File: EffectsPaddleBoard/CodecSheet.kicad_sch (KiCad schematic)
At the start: 1 part, among them U3 TLV320AIC3100

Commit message: Added power to uC, but overall power not finished
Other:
- company: (none) -> Selbstständig
- title: (none) -> Effects Paddle
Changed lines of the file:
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@@
 (kicad_sch (version 20230121) (generator eeschema)
   (paper "A4")
+  (title_block
+    (title "Effects Paddle")
+    (date "2023-07-01")
+    (rev "0.1")
+    (company "Selbstständig")
+  )
   (symbol (lib_id "Audio:TLV320AIC3100") (at 158.75 99.06 0) (unit 1)
     (in_bom yes) (on_board yes) (dnp no) (fields_autoplaced)

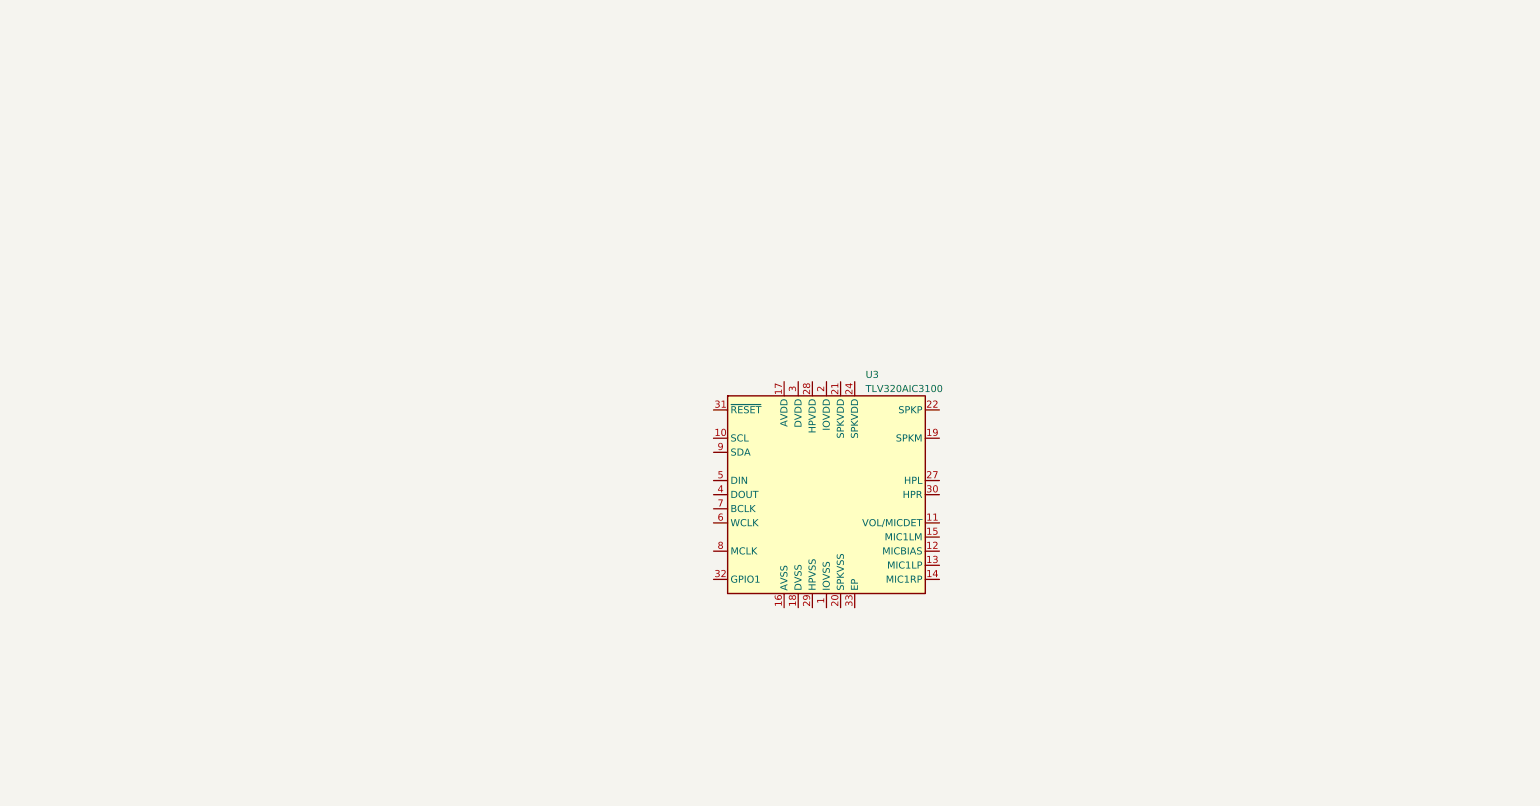
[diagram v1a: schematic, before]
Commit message: While wiring the codec, I found that I used the wrong controller and so I2S communication is unidirectional only: TODO: fix that
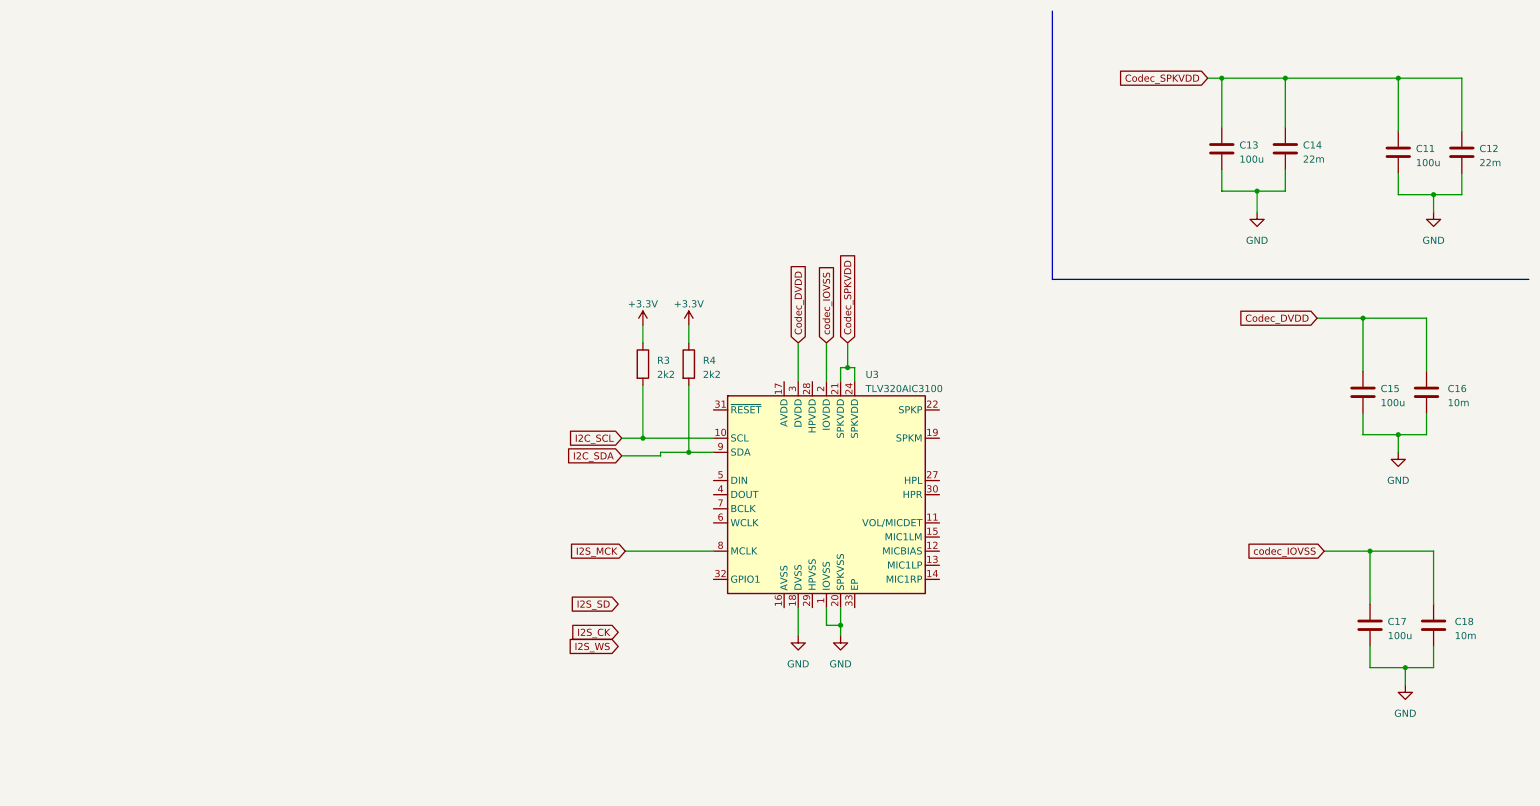
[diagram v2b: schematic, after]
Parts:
- added C11, C13, C15, C17: 100u, symbol Device:C
- added C12, C14: 22m, symbol Device:C
- added C16, C18: 10m, symbol Device:C
- added R3, R4: 2k2, symbol Device:R
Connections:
- net GND: now reaches U3.1 (IOVSS)
- net GND: now also U3.18 (DVSS), U3.20 (SPKVSS), U3.25 (SPKVSS), C11.2, C12.2, C13.2, C14.2, C15.2, C16.2, C17.2, C18.2
- net I2C_SCL: now reaches U3.10 (SCL)
- net I2C_SCL: now also R3.2
- net codec_IOVSS: now reaches U3.2 (IOVDD)
- net codec_IOVSS: now also C17.1, C18.1
- net Codec_SPKVDD: now reaches U3.21 (SPKVDD)
- net Codec_SPKVDD: now also U3.24 (SPKVDD), C11.1, C12.1, C13.1, C14.1
- net Codec_DVDD: now reaches U3.3 (DVDD)
- net Codec_DVDD: now also C15.1, C16.1
- net I2S_MCK: now reaches U3.8 (MCLK)
- net I2C_SDA: now reaches U3.9 (SDA)
- net I2C_SDA: now also R4.2
- new net +3.3V: R3.1, R4.1

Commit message: Added power supply
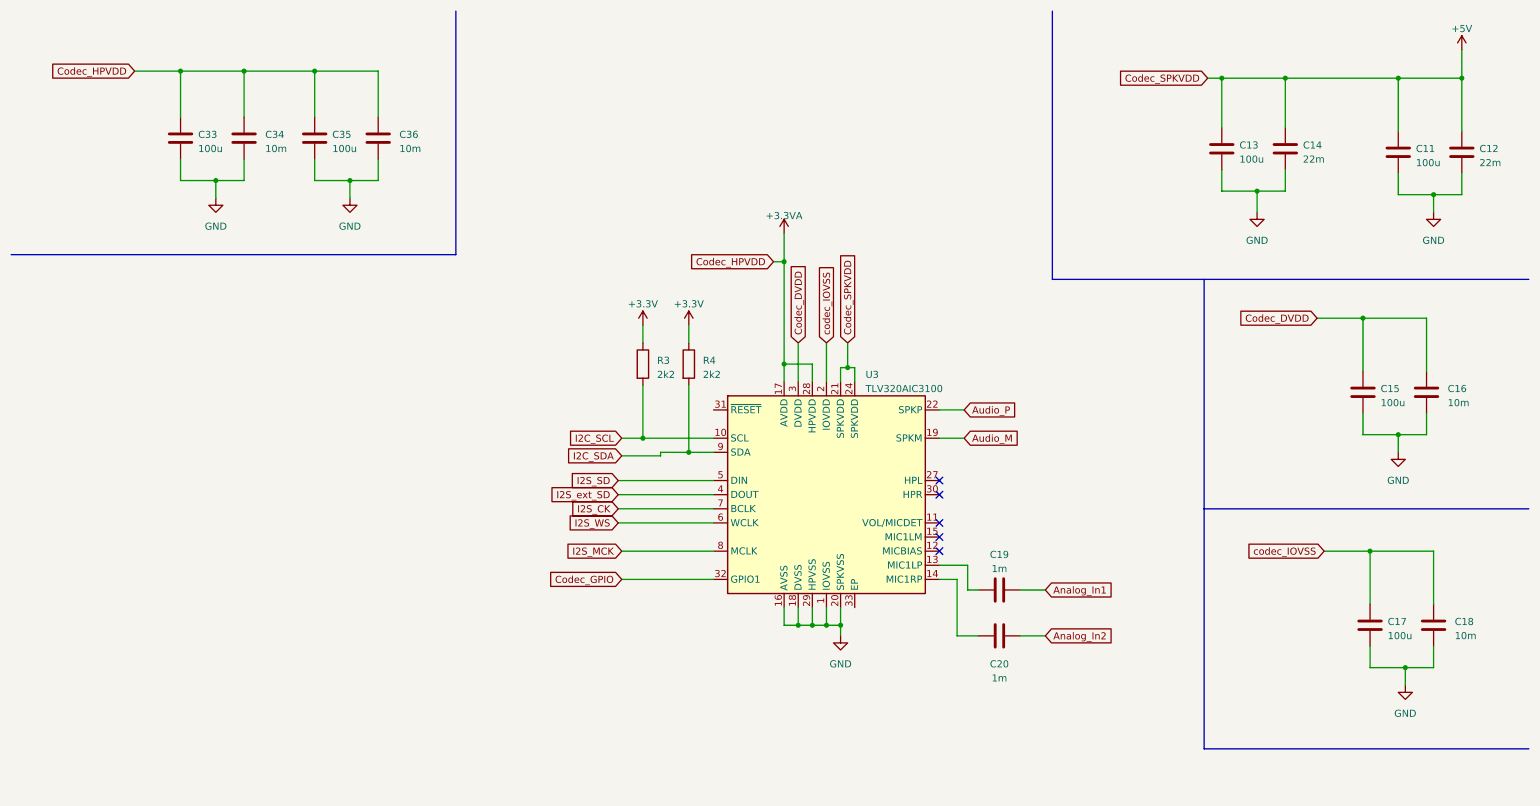
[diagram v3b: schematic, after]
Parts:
- added C19, C20: 1m, symbol Device:C
- added C33, C35: 100u, symbol Device:C
- added C34, C36: 10m, symbol Device:C
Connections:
- net GND: now also U3.16 (AVSS), U3.29 (HPVSS), C33.2, C34.2, C35.2, C36.2
- net I2S_CK: now also U3.7 (BCLK)
- net I2S_SD: now also U3.5 (DIN)
- net I2S_WS: now also U3.6 (WCLK)
- net at U3.13 (MIC1LP): now also C19.1
- net at U3.14 (MIC1RP): now also C20.1
- net +3.3VA: now reaches U3.17 (AVDD)
- net +3.3VA: now also U3.28 (HPVDD), C33.1, C34.1, C35.1, C36.1
- net Audio_M: now reaches U3.19 (SPKM), U3.23 (SPKM)
- net Audio_P: now reaches U3.22 (SPKP), U3.26 (SPKP)
- net Codec_GPIO: now reaches U3.32 (GPIO1)
- net I2S_ext_SD: now reaches U3.4 (DOUT)
- net Codec_SPKVDD renamed +5V
- new net Analog_In1: C19.2
- new net Analog_In2: C20.2
- no-connect marks 0 -> 5

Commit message: Finished schematic
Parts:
- added R16, R17, R18, R19, R20: 10k, symbol Device:R
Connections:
- net codec_IOVSS is gone; now on net +3.3V: C17.1, C18.1, U3.2 (IOVDD)
- net GND: now also R16.2, R17.2, R18.2, R19.2, R20.2
- net at U3.11 (VOL/MICDET): now also R18.1
- net at U3.12 (MICBIAS): now also R16.1
- net at U3.15 (MIC1LM): now also R17.1
- net at U3.27 (HPL): now also R20.1
- net at U3.30 (HPR): now also R19.1
- net Codec_DVDD renamed +1V8
- no-connect marks 5 -> 0
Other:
- moved on the sheet: C19, C20, R3, R4, U3

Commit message: Began with pcb layout
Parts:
- C11: footprint (none) -> Capacitor_SMD:C_0402_1005Metric
- C12, C13, C14, C15, C16, C17, C18, C19, C20, C33, C34, C35, C36: footprint (none) -> Capacitor_SMD:C_1206_3216Metric
- R16, R17, R18, R19, R20, R3, R4: footprint (none) -> Resistor_SMD:R_0402_1005Metric

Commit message: Reviev by David and netnaming
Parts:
- C11: footprint Capacitor_SMD:C_0402_1005Metric -> Capacitor_SMD:C_1206_3216Metric
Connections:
- net GND: now also U3.33 (EP)
- net Analog_In_R: now reaches C20.1, U3.14 (MIC1RP)
- net MIC1LM: now reaches R17.1, U3.15 (MIC1LM)
- net HPL: now reaches R20.1, U3.27 (HPL)
- net Volume: now reaches R18.1, U3.11 (VOL/MICDET)
- net MICBIAS: now reaches R16.1, U3.12 (MICBIAS)
- net Analog_In_L: now reaches C19.1, U3.13 (MIC1LP)
- net HPR: now reaches R19.1, U3.30 (HPR)
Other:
- note added: "is termination needed?"
- note added: "reset anhängen"
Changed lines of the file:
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@@
+    (stroke (width 0) (type default))
+  )
+  (wire (pts (xy 122.555 139.065) (xy 120.015 139.065))
     (stroke (width 0) (type default))
   )
@@
     (stroke (width 0) (type default))
   )
+  (wire (pts (xy 122.555 135.89) (xy 122.555 139.065))
+    (stroke (width 0) (type default))
+  )
   (wire (pts (xy 267.97 107.315) (xy 267.97 109.22))
     (stroke (width 0) (type default))
@@
   (wire (pts (xy 229.87 24.13) (xy 241.3 24.13))
     (stroke (width 0) (type default))
+  )
+  (text "is termination needed?" (at 38.735 117.475 0)
+    (effects (font (size 1.27 1.27)) (justify left bottom))
+  )
+  (text "reset anhängen" (at 61.595 96.52 0)
+    (effects (font (size 1.27 1.27)) (justify left bottom))
+  )
+  (label "Analog_In_R" (at 140.97 142.24 180) (fields_autoplaced)
+    (effects (font (size 1.27 1.27)) (justify right bottom))
+  )
+  (label "Volume" (at 145.415 120.65 0) (fields_autoplaced)
+    (effects (font (size 1.27 1.27)) (justify left bottom))
+  )
+  (label "Analog_In_L" (at 139.065 128.27 0) (fields_autoplaced)
+    (effects (font (size 1.27 1.27)) (justify left bottom))
+  )
+  (label "MIC1LM" (at 144.78 123.19 0) (fields_autoplaced)
+    (effects (font (size 1.27 1.27)) (justify left bottom))
+  )
+  (label "HPL" (at 144.145 113.03 0) (fields_autoplaced)
+    (effects (font (size 1.27 1.27)) (justify left bottom))
+  )
+  (label "MICBIAS" (at 144.78 125.73 0) (fields_autoplaced)
+    (effects (font (size 1.27 1.27)) (justify left bottom))
+  )
+  (label "HPR" (at 144.145 115.57 0) (fields_autoplaced)
+    (effects (font (size 1.27 1.27)) (justify left bottom))
   )
   (global_label "I2C_SCL" (shape input) (at 80.645 105.41 180) (fields_autoplaced)
@@
       (effects (font (size 1.27 1.27)) (justify left))
     )
-    (property "Footprint" "Capacitor_SMD:C_0402_1005Metric" (at 262.5852 41.275 0)
+    (property "Footprint" "Capacitor_SMD:C_1206_3216Metric" (at 262.5852 41.275 0)
       (effects (font (size 1.27 1.27)) hide)
     )
@@
   )
   (symbol (lib_id "Device:C") (at 149.225 133.985 90) (unit 1)
-    (in_bom yes) (on_board yes) (dnp no) (fields_autoplaced)
-    (property "Reference" "C19" (at 149.225 127.635 90)
-      (effects (font (size 1.27 1.27)))
-    )
+    (in_bom yes) (on_board yes) (dnp no)
+    (property "Reference" "C19" (at 153.67 130.81 90)
+      (effects (font (size 1.27 1.27)))
+    )

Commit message: Finished layout
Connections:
- net Codec_Reset: now reaches U3.31 (~{RESET})
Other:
- note removed: "reset anhängen"
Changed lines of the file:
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@@
+    (stroke (width 0) (type default))
+  )
+  (wire (pts (xy 97.155 100.33) (xy 80.01 100.33))
     (stroke (width 0) (type default))
   )
@@
   )
   (text "is termination needed?" (at 38.735 117.475 0)
-    (effects (font (size 1.27 1.27)) (justify left bottom))
-  )
-  (text "reset anhängen" (at 61.595 96.52 0)
     (effects (font (size 1.27 1.27)) (justify left bottom))
   )
@@
       (effects (font (size 1.27 1.27)) (justify right) hide)
     )
+  )
+  (global_label "Codec_Reset" (shape input) (at 80.01 100.33 180) (fields_autoplaced)
+    (effects (font (size 1.27 1.27)) (justify right))
+    (property "Intersheetrefs" "${INTERSHEET_REFS}" (at 65.1904 100.33 0)
+      (effects (font (size 1.27 1.27)) (justify right) hide)
+    )
